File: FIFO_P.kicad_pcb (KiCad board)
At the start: 4 copper layers, 70 parts, among them J1 Vin +, J2 Vin -, J3 Conn_Coaxial, J4 Jack-DC, SW1 Rotary_Encoder_61C, U1 SN74LVC2G157_MUX_TI, U10 AD7840, U11 LM2940CT-5.0, U12 UA79M05CKCS_-5V, U13 LM2940CT-3.3, U2 IDT_ICS551, U3 LTC1740, U4 ARDUINO_DUE_FIFO_P_COMMANDS, U5 IDT_72V2105, U6 TXB0104, U7 TXB0104, U8 TXB0104, U9 TXB0104

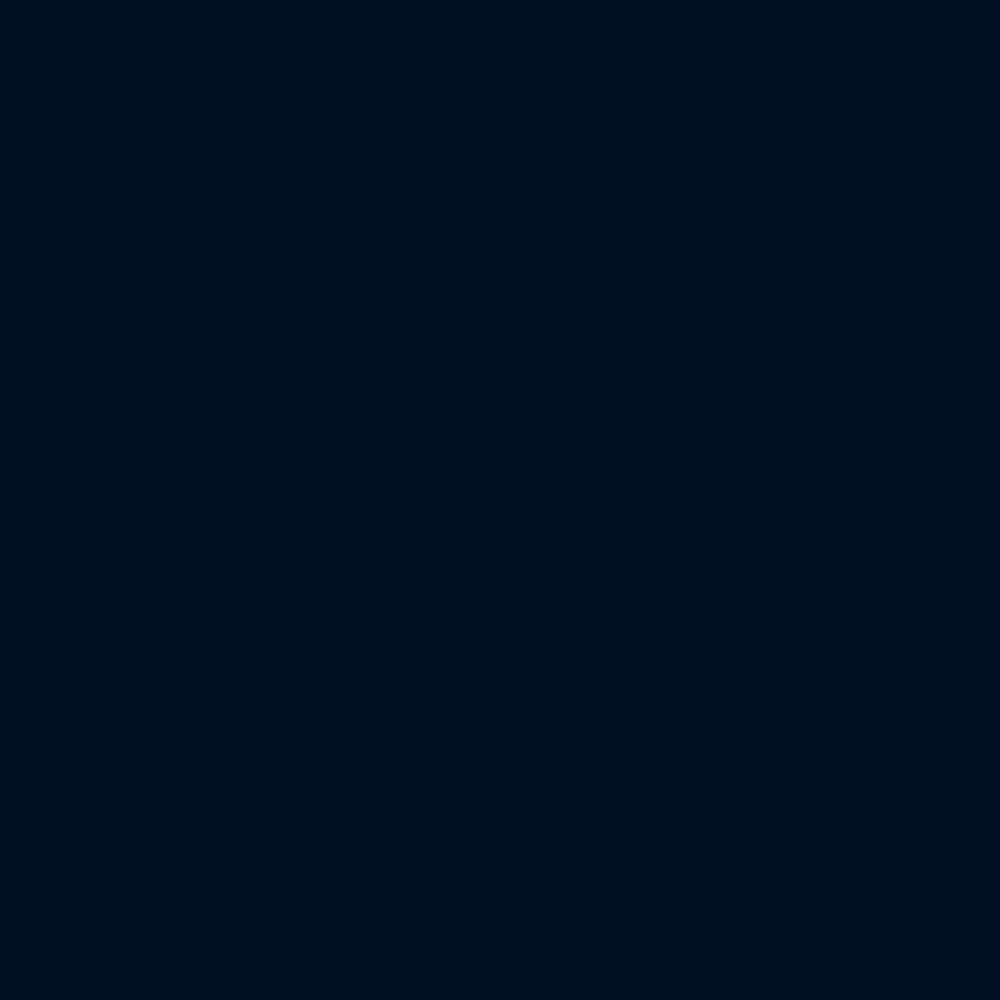
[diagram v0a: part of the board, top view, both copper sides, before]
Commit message: Created 4-layer PCB
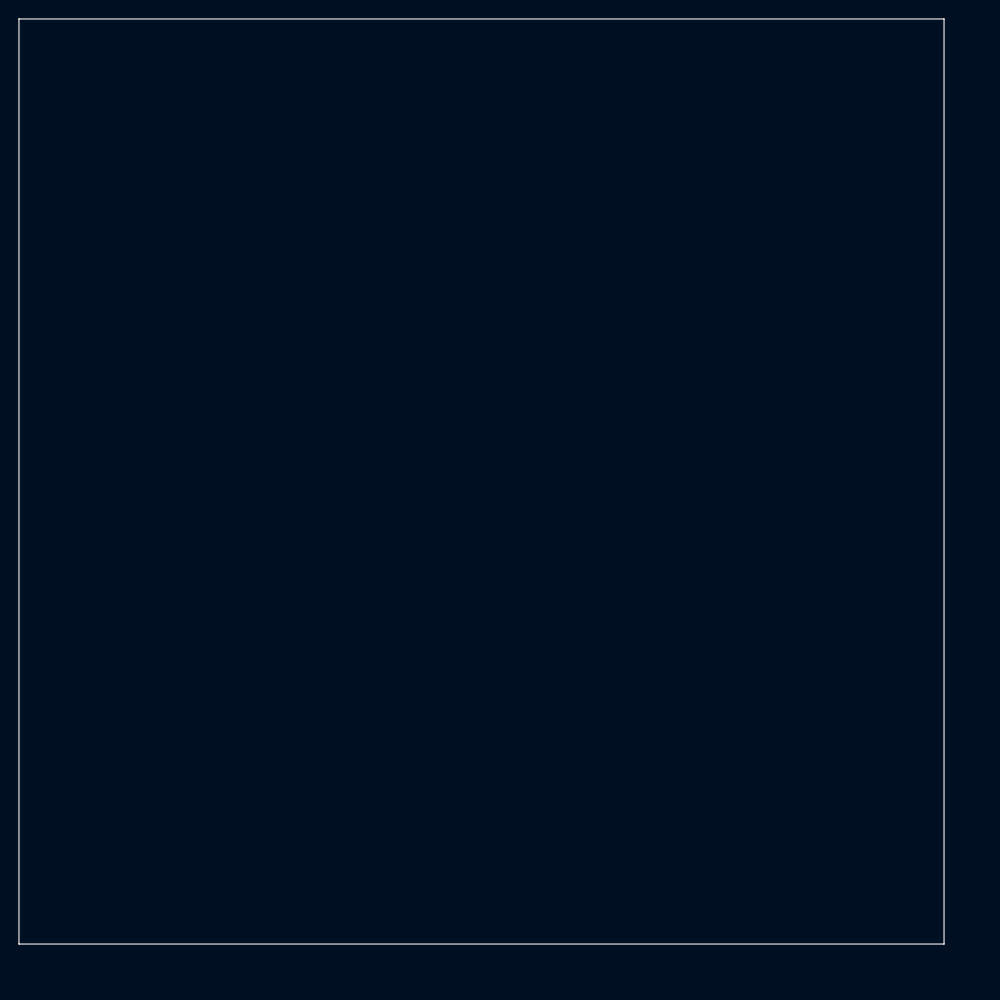
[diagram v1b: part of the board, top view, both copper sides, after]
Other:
- board outline added: 100 x 100 mm
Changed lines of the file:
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@@
   (general
     (thickness 1.6)
-    (drawings 0)
+    (drawings 4)
     (tracks 0)
     (zones 0)
@@
     )
   )
+  (gr_line (start 17 117) (end 17 17) (layer Edge.Cuts) (width 0.1))
+  (gr_line (start 117 117) (end 17 117) (layer Edge.Cuts) (width 0.1))
+  (gr_line (start 117 17) (end 117 117) (layer Edge.Cuts) (width 0.1))
+  (gr_line (start 17 17) (end 117 17) (layer Edge.Cuts) (width 0.1))
 )

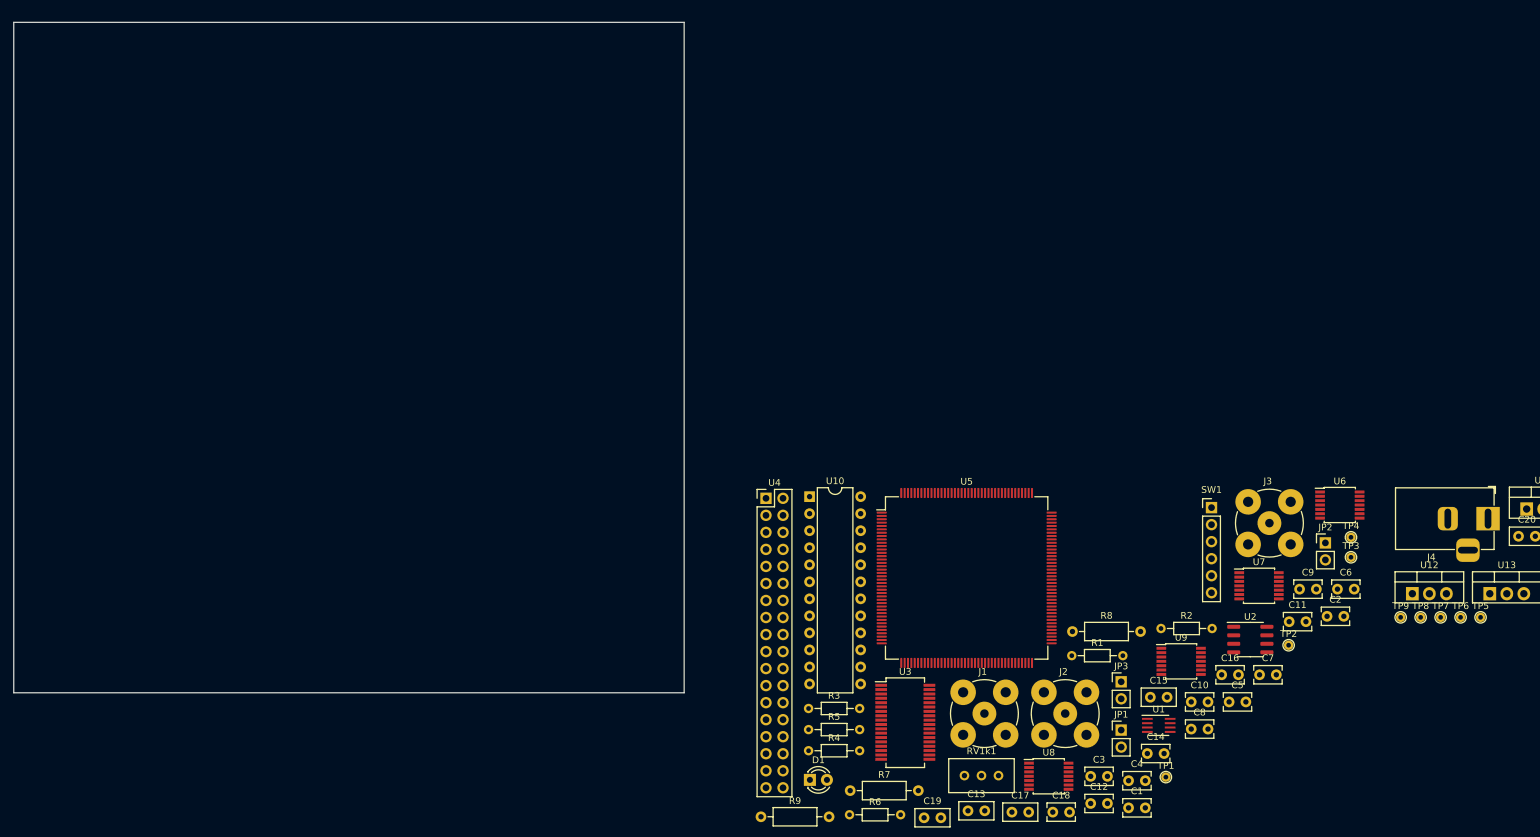
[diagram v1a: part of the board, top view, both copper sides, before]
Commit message: Fix arduino header, started laying out connectors
The pins used were changed, so the old code must be rewritten to use the new pins and port D instead of port A.
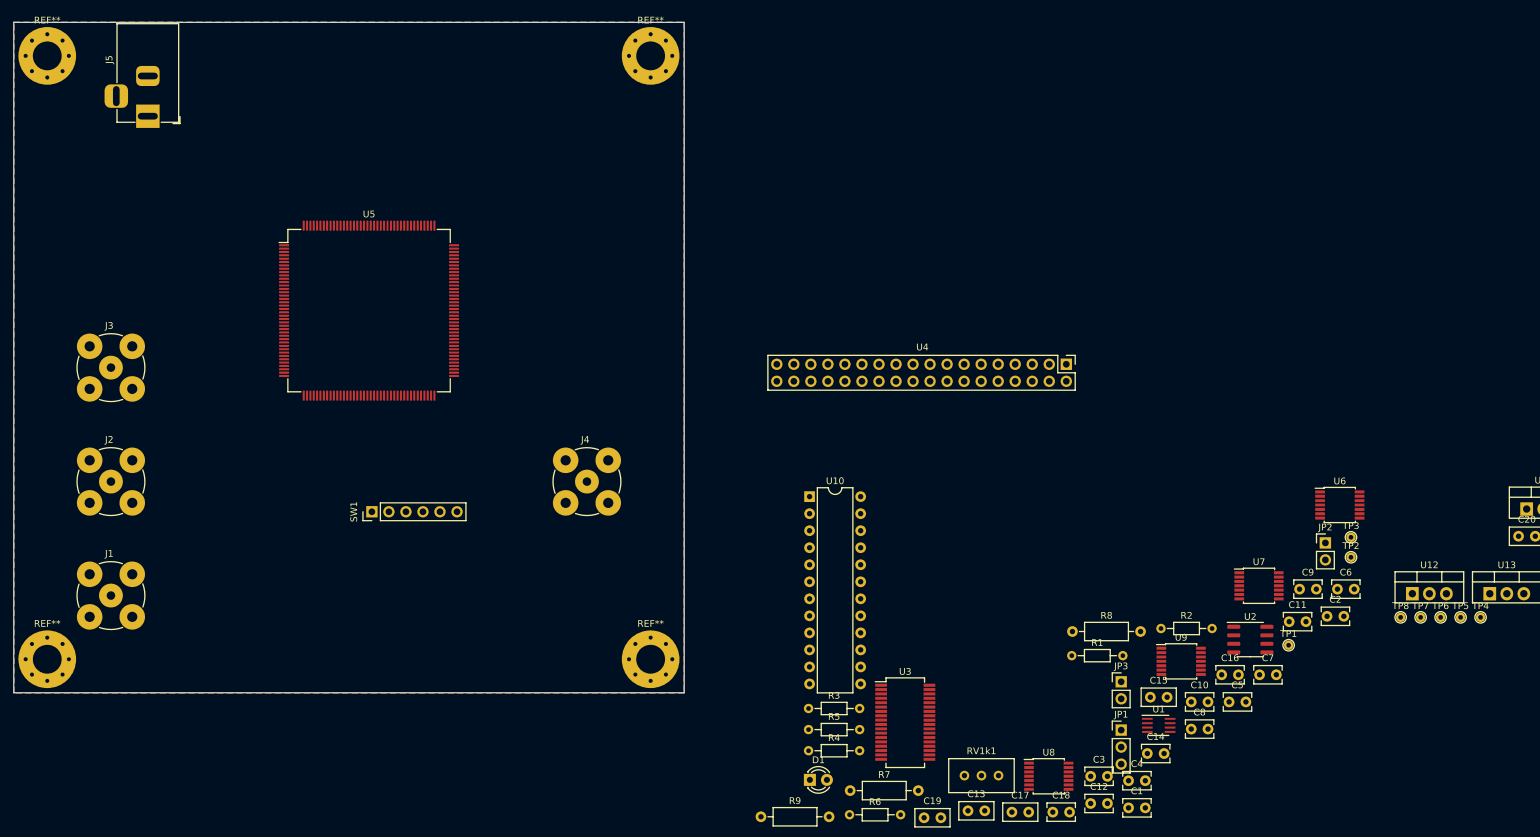
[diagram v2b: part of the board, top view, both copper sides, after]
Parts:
- removed the TP1 at (188.9, 129.6)
- added J3: ICLK, Connector_Coaxial:BNC_TEConnectivity_1478204_Vertical, F.Cu at (31.5, 68.5)
- added REF**: MountingHole_4.3mm_M4_Pad_Via, MountingHole:MountingHole_4.3mm_M4_Pad_Via, F.Cu at (22.0, 22.0)
- added REF**: MountingHole_4.3mm_M4_Pad_Via, MountingHole:MountingHole_4.3mm_M4_Pad_Via, F.Cu at (112.0, 22.0)
- added REF**: MountingHole_4.3mm_M4_Pad_Via, MountingHole:MountingHole_4.3mm_M4_Pad_Via, F.Cu at (112.0, 112.0)
- added REF**: MountingHole_4.3mm_M4_Pad_Via, MountingHole:MountingHole_4.3mm_M4_Pad_Via, F.Cu at (22.0, 112.0)
- J4: renamed from J3; value Conn_Coaxial -> Vout
- JP1: footprint Connector_PinHeader_2.54mm:PinHeader_1x02_P2.54mm_Vertical -> Connector_PinHeader_2.54mm:PinHeader_1x03_P2.54mm_Vertical
- moved J5 208.7 mm to (37.0, 31.0), turned to 270 degrees
- moved J2 146.5 mm to (31.5, 85.5)
- moved J1 131.5 mm to (31.5, 102.5)
- moved SW1 125.2 mm to (70.4, 90.0), turned to 90 degrees
- moved J4 102.0 mm to (102.5, 85.5)
- moved U5 97.6 mm to (70.0, 60.0)
- moved U4 49.1 mm to (174.0, 68.0)
- renumbered J4 to J5, TP2 to TP1, TP3 to TP2, TP4 to TP3, TP5 to TP4, TP6 to TP5, TP7 to TP6, TP8 to TP7, TP9 to TP8
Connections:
- U4 pad 25: Net-(U4-Pad25) -> Net-(R9-Pad2)
- U4 pad 26: Net-(U4-Pad26) -> Net-(R7-Pad2)
- U4 pad 28: Net-(U4-Pad28) -> Net-(R8-Pad2)
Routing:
- added copper zone on F.Cu, net +5V
- added copper zone on B.Cu, net -5V
- added copper zone on In2.Cu, net 3.3V
- added copper zone on In1.Cu, net GND

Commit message: ADC to FIFO routing
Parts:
- removed REF** (x4): MountingHole_4.3mm_M4_Pad_Via, MountingHole:MountingHole_4.3mm_M4_Pad_Via
- U5: footprint Package_QFP:LQFP-160_24x24mm_P0.5mm -> Package_QFP:LQFP-64_14x14mm_P0.8mm
- moved C6 195.9 mm to (25.0, 51.8), turned to 90 degrees
- moved C9 193.3 mm to (22.0, 51.8), turned to 90 degrees
- moved C5 189.6 mm to (25.0, 41.5), turned to 270 degrees
- moved C8 188.8 mm to (22.0, 41.5), turned to 270 degrees
- moved U2 179.9 mm to (31.5, 50.0), turned to 180 degrees
- moved U1 175.3 mm to (31.5, 42.5), turned to 180 degrees
- moved C2 168.3 mm to (51.0, 59.5), turned to 270 degrees
- moved R2 166.3 mm to (22.5, 93.0), turned to 90 degrees
- moved R1 152.3 mm to (22.5, 110.1), turned to 90 degrees
- moved JP1 145.2 mm to (43.8, 78.8), turned to 180 degrees
- moved C12 142.3 mm to (65.0, 46.5), turned to 270 degrees
- moved C3 140.8 mm to (54.0, 62.0), turned to 90 degrees
- moved C13 130.8 mm to (65.0, 44.0), turned to 180 degrees
- moved U4 130.3 mm to (50.0, 28.0), turned to 180 degrees
- moved R6 127.9 mm to (40.5, 57.0), turned to 90 degrees
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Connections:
- U1 pad 3: Net-(U1-Pad3) -> (no net)
- U3 pad 18: Net-(U3-Pad18) -> (no net)
- U3 pad 27: Net-(U3-Pad27) -> (no net)
- U4 pad 30: Net-(U4-Pad30) -> (no net)
- U4 pad 31: Net-(U4-Pad31) -> (no net)
- U4 pad 32: Net-(U4-Pad32) -> (no net)
- U4 pad 33: Net-(U4-Pad33) -> (no net)
- U4 pad 35: Net-(U4-Pad35) -> (no net)
- U4 pad 36: Net-(U4-Pad36) -> (no net)
- U4 pad 43: Net-(U4-Pad43) -> (no net)
- U4 pad 52: Net-(U4-Pad52) -> (no net)
- U5 pad 20: Net-(U5-Pad20) -> (no net)
- U5 pad 21: Net-(U5-Pad21) -> (no net)
- U5 pad 22: Net-(U5-Pad22) -> (no net)
- U5 pad 25: Net-(U5-Pad25) -> (no net)
- U5 pad 26: Net-(U5-Pad26) -> (no net)
- U5 pad 28: Net-(U5-Pad28) -> (no net)
- U5 pad 29: Net-(U5-Pad29) -> (no net)
- U6 pad 6: Net-(U6-Pad6) -> (no net)
- U6 pad 9: Net-(U6-Pad9) -> (no net)
- U7 pad 6: Net-(U7-Pad6) -> (no net)
- U7 pad 9: Net-(U7-Pad9) -> (no net)
- U8 pad 6: Net-(U8-Pad6) -> (no net)
- U8 pad 9: Net-(U8-Pad9) -> (no net)
- U9 pad 10: Net-(U9-Pad10) -> (no net)
- U9 pad 6: Net-(U9-Pad6) -> (no net)
- U9 pad 9: Net-(U9-Pad9) -> (no net)
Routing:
- net 3.3V: track 0.00 -> 39.6 mm, vias 0 -> 10
- net LDAC5V: track 0.00 -> 36.5 mm
- net +5V: track 0.00 -> 34.3 mm
- net Net-(J2-Pad1): track 0.00 -> 28.4 mm
- net Net-(U10-Pad17): track 0.00 -> 28.0 mm
- net Net-(J3-Pad1): track 0.00 -> 27.9 mm
- net GND: track 0.00 -> 26.9 mm, vias 0 -> 4
- net Net-(U10-Pad16): track 0.00 -> 24.5 mm
- net Net-(U10-Pad15): track 0.00 -> 22.5 mm
- net Net-(U3-Pad26): track 0.00 -> 18.4 mm
- net Net-(U3-Pad25): track 0.00 -> 17.7 mm
- net Net-(J1-Pad1): track 0.00 -> 17.5 mm
- net Net-(U3-Pad24): track 0.00 -> 16.9 mm
- net Net-(U3-Pad23): track 0.00 -> 16.1 mm
- net Net-(U3-Pad12): track 0.00 -> 15.8 mm
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
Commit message: Most routing done
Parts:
- added REF** (x2): MountingHole_3.2mm_M3_ISO14580, MountingHole:MountingHole_3.2mm_M3_ISO14580, F.Cu at (62.5, 71.0)
- added REF**: MountingHole_4.3mm_M4_Pad_Via, MountingHole:MountingHole_4.3mm_M4_Pad_Via, F.Cu at (144.5, 54.5)
- added REF**: MountingHole_4.3mm_M4_Pad_Via, MountingHole:MountingHole_4.3mm_M4_Pad_Via, F.Cu at (144.5, 144.5)
- added REF**: MountingHole_4.3mm_M4_Pad_Via, MountingHole:MountingHole_4.3mm_M4_Pad_Via, F.Cu at (54.5, 144.5)
- added REF**: MountingHole_4.3mm_M4_Pad_Via, MountingHole:MountingHole_4.3mm_M4_Pad_Via, F.Cu at (54.5, 54.5)
- R7, R8, R9, U10, U4, U6, U7, U8, U9: moved to B.Cu
- U11, U13: footprint Package_TO_SOT_THT:TO-220-3_Vertical -> Package_TO_SOT_THT:TO-220-3_Horizontal_TabDown
- moved C24 199.1 mm to (55.5, 94.2), turned to 180 degrees
- moved C29 198.7 mm to (55.5, 97.2), turned to 180 degrees
- moved C28 198.6 mm to (55.5, 100.2), turned to 180 degrees
- moved C21 197.6 mm to (55.5, 81.5), turned to 180 degrees
- moved C25 192.3 mm to (55.5, 91.2), turned to 180 degrees
- moved C20 186.6 mm to (55.5, 78.5), turned to 180 degrees
- moved U13 178.9 mm to (58.5, 92.8), turned to 270 degrees
- moved TP6 176.7 mm to (54.2, 86.2)
- moved TP4 170.6 mm to (69.5, 67.5)
- moved TP8 168.4 mm to (55.5, 103.5)
- moved U11 126.5 mm to (58.5, 80.0), turned to 270 degrees
- moved U4 125.7 mm to (139.2, 116.5), turned to 270 degrees
- moved TP3 119.0 mm to (102.5, 128.0)
- moved C8 116.5 mm to (136.0, 65.5), turned to 180 degrees
- moved C5 114.2 mm to (136.0, 68.5), turned to 180 degrees
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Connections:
- U9 pad 5: Net-(U9-Pad5) -> GND
- U9 pad 7: Net-(U9-Pad5) -> GND
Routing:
- net Net-(U10-Pad24): track 0.00 -> 110.5 mm, vias 0 -> 1
- net Net-(U10-Pad1): track 0.00 -> 85.9 mm, vias 0 -> 2
- net Net-(U4-Pad24): track 0.00 -> 56.3 mm
- net LDAC: track 0.00 -> 41.5 mm, vias 0 -> 3
- net Net-(R7-Pad2): track 0.00 -> 39.9 mm
- net 3.3V: track 39.6 -> 76.8 mm, vias 10 -> 11
- net Net-(R8-Pad2): track 0.00 -> 36.2 mm
- net RCLK: track 0.00 -> 35.1 mm, vias 0 -> 2
- net Net-(R9-Pad2): track 0.00 -> 31.0 mm, vias 0 -> 2
- net WCLK: track 0.00 -> 30.7 mm, vias 0 -> 2
- net +5V: track 34.3 -> 58.5 mm
- net GND: track 26.9 -> 49.5 mm, vias 4 -> 11
- net Net-(U4-Pad23): track 0.00 -> 22.3 mm
- net WLSTN: track 0.00 -> 21.7 mm
- net Net-(U4-Pad27): track 0.00 -> 20.5 mm
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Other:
- board text added: "APPROX"
